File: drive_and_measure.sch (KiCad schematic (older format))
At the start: 39 parts, among them J10 Conn_Coaxial, J17 Conn_Coaxial, J2 7461057, J3 7461057, J4 7461057, J5 7461057, Q1 2SC5242, Q2 2SC5242, Q3 2SD882, U2 INA240A2D, U5 OPA188xxDBV

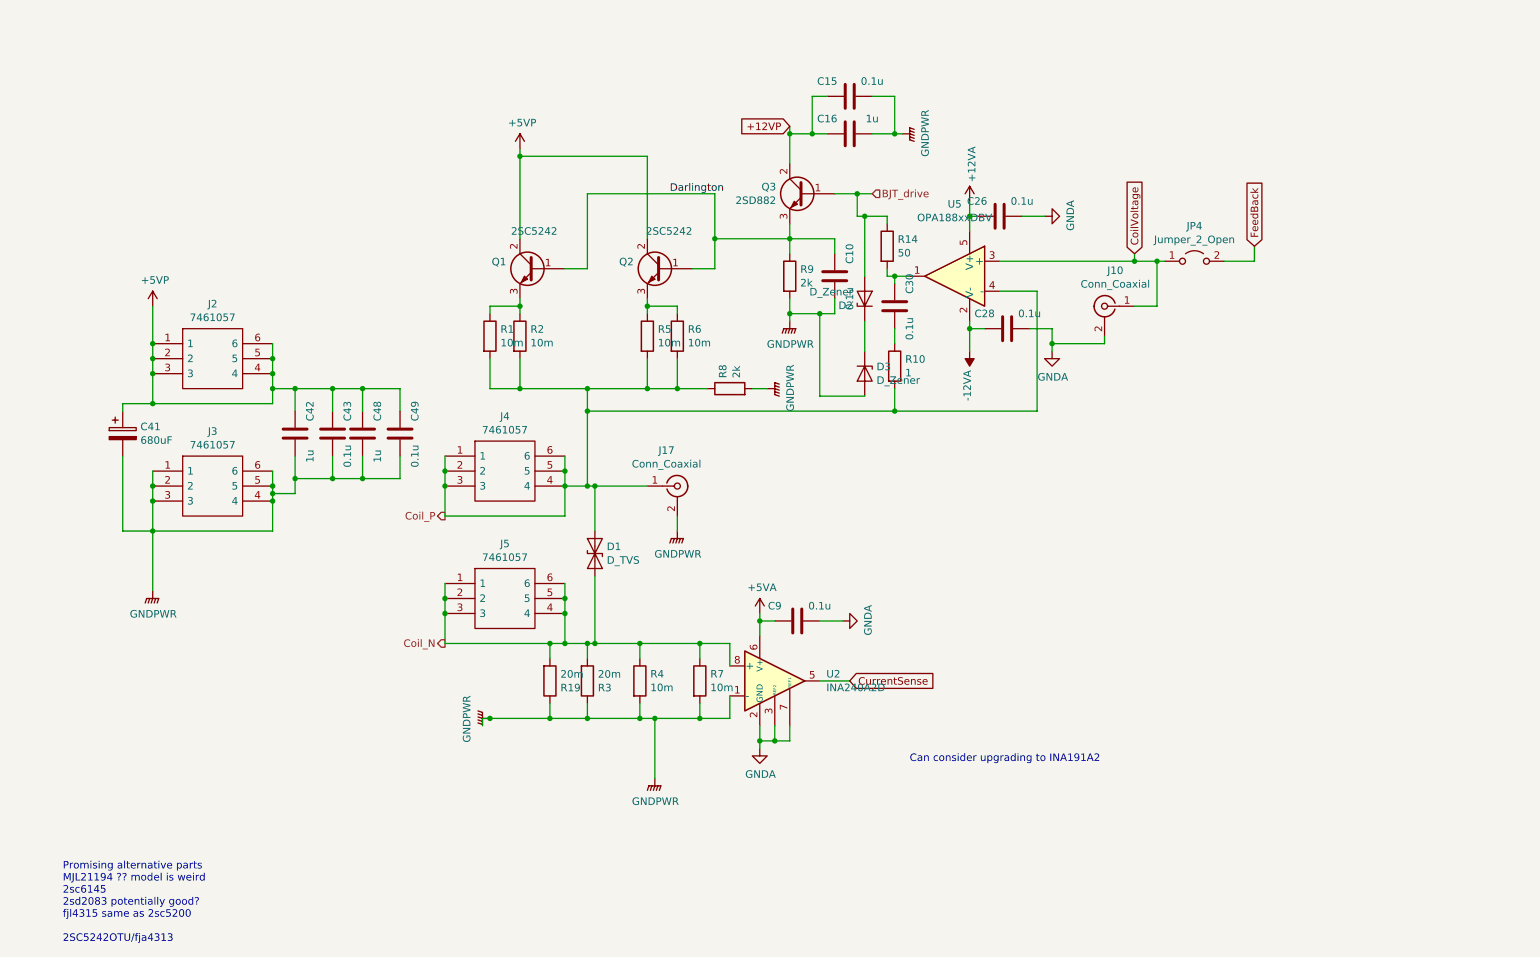
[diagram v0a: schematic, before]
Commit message: Updated design, to include proper feedback and a current bias. Note the sign of the feedback might still be problematic. Need to be checked again
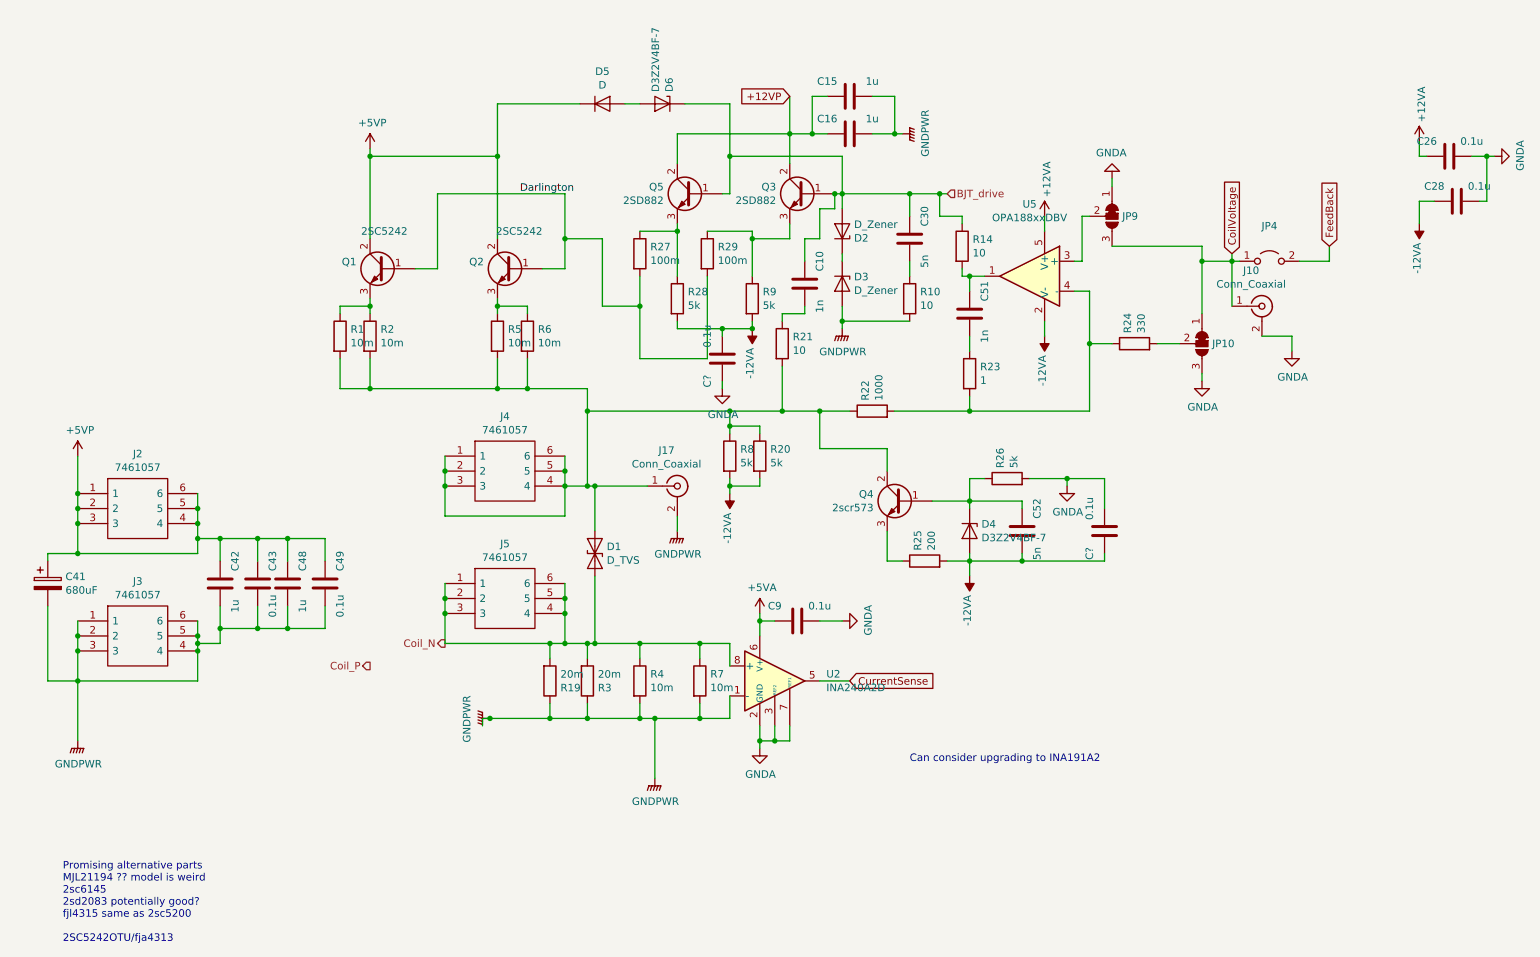
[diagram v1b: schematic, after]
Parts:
- added C51: 1n, Capacitor_SMD:C_1206_3216Metric, symbol Device:C
- added C52: 5n, Capacitor_SMD:C_1206_3216Metric, symbol Device:C
- added C? (x2): 0.1u, Capacitor_SMD:C_0805_2012Metric_Pad1.15x1.40mm_HandSolder, symbol Device:C
- added D4, D6: D3Z2V4BF-7, Diode_SMD:D_SOD-323, symbol Device:D_Zener
- added D5: D, Diode_SMD:D_SOD-323, symbol Device:D
- added JP10, JP9: SolderJumper_3_Bridged12, Jumper:SolderJumper-3_P1.3mm_Bridged12_RoundedPad1.0x1.5mm, symbol Jumper:SolderJumper_3_Bridged12
- added Q4: 2scr573, Package_TO_SOT_SMD:TO-252-2, symbol Device:Q_NPN_BCE
- added Q5: 2SD882, Package_TO_SOT_THT:TO-126-3_Horizontal_TabDown, symbol Device:Q_NPN_BCE
- added R20, R26, R28: 5k, Resistor_SMD:R_1206_3216Metric_Pad1.42x1.75mm_HandSolder, symbol Device:R
- added R21: 10, Resistor_SMD:R_1206_3216Metric_Pad1.42x1.75mm_HandSolder, symbol Device:R
- added R22: 1000, Resistor_SMD:R_1206_3216Metric_Pad1.42x1.75mm_HandSolder, symbol Device:R
- added R23: 1, Resistor_SMD:R_1206_3216Metric_Pad1.42x1.75mm_HandSolder, symbol Device:R
- added R24: 330, Resistor_SMD:R_1206_3216Metric_Pad1.42x1.75mm_HandSolder, symbol Device:R
- added R25: 200, Resistor_SMD:R_1206_3216Metric_Pad1.42x1.75mm_HandSolder, symbol Device:R
- added R27, R29: 100m, Resistor_SMD:R_1206_3216Metric_Pad1.42x1.75mm_HandSolder, symbol Device:R
- C10: value 0.1u -> 1n
- C15: value 0.1u -> 1u; footprint Capacitor_SMD:C_0805_2012Metric_Pad1.15x1.40mm_HandSolder -> Capacitor_SMD:C_1206_3216Metric_Pad1.42x1.75mm_HandSolder
- C30: value 0.1u -> 5n
- Q1, Q2: footprint Package_TO_SOT_THT:TO-3P-3_Horizontal_TabDown -> Package_TO_SOT_THT:TO-3P-3_Vertical
- R10: value 1 -> 10
- R14: value 50 -> 10
- R8, R9: value 2k -> 5k
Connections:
- net +12VP: now also Q5.2 (C)
- net +5VP: now also D5.1 (K)
- net -12VA: now also R8.2, R9.2, C52.1, C?.1, C?.2, D4.2 (A), R20.2, R25.2, R28.2
- net BJT_drive: now also C10.2, C30.2, D6.1 (K), Q5.1 (B)
- net CoilVoltage: now also JP10.1 (A), JP9.3 (B); no longer U5.3 (+)
- net Coil_P: no longer D1.1 (A1), J17.1 (In), J4.1, J4.2, J4.3, J4.4, J4.5, J4.6, R1.2, R10.2, R2.2, R5.2, R6.2, R8.1, U5.4 (-)
- net Darlington: now also R27.2, R29.2; no longer C10.2, Q3.3 (E), R9.1
- net GNDA: now also C?.1, C?.2, JP10.3 (B), JP9.1 (A), R26.2
- net GNDPWR: now also R10.2; no longer C10.1, R8.2, R9.2
- net at R14.2, U5.1: now also C51.2; no longer C30.2
- new net: D1.1 (A1), J17.1 (In), J4.1, J4.2, J4.3, J4.4, J4.5, J4.6, Q4.2 (C), R1.2, R2.2, R20.1, R21.2, R22.1, R5.2, R6.2, R8.1
- new net: Q3.3 (E), R29.1, R9.1
- new net: JP9.2 (C), U5.3 (+)
- new net: R22.2, R23.2, R24.1, U5.4 (-)
- new net: JP10.2 (C), R24.2
- new net: C51.1, R23.1
- new net: D5.2 (A), D6.2 (A)
- new net: C10.1, R21.1
- new net: C52.2, D4.1 (K), Q4.1 (B), R26.1
- new net: Q4.3 (E), R25.1
- new net: Q5.3 (E), R27.1, R28.1
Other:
- moved on the sheet: C26, C28, C41, C42, C43, C48, C49, D2, D3, J10, J2, J3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

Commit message: Allowed swapping feedback signs
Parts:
- added C?: 680uF, Capacitor_THT:CP_Radial_D8.0mm_P3.80mm, symbol Device:CP
- gave numbers to parts that had none: 2
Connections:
- net Coil_P: now also D1.1 (A1), J17.1 (In), J4.1, J4.2, J4.3, J4.4, J4.5, J4.6, Q4.2 (C), R1.2, R2.2, R20.1, R21.2, R22.1, R5.2, R6.2, R8.1
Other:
- moved on the sheet: C41, C42, C43, C48, C49, J2, J3

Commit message: Design a common-mode choke / filter for the controller analog supplies. Avoid using one AC/DC converter for each board, but also suppress ground loops
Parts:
- C41: footprint Capacitor_THT:CP_Radial_D8.0mm_P3.80mm -> SamacSys_Parts:CP_Radial_D10.0mm_P3.5_5
- C55: renamed from C?; value 680uF -> 2000uF; footprint Capacitor_THT:CP_Radial_D8.0mm_P3.80mm -> Capacitor_THT:CP_Radial_D10.0mm_P5.00mm
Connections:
- net +5VP: now also C55.1
- net GNDPWR: now also C55.2
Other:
- moved on the sheet: C55
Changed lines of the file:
@@
 EESchema Schematic File Version 4
-LIBS:shunt_current_control_v2-cache
 EELAYER 30 0
 EELAYER END
@@
 F 0 "C41" H 1168 4496 50  0000 L CNN
 F 1 "680uF" H 1168 4405 50  0000 L CNN
-F 2 "Capacitor_THT:CP_Radial_D8.0mm_P3.80mm" H 1088 4300 50  0001 C CNN
+F 2 "SamacSys_Parts:CP_Radial_D10.0mm_P3.5_5" H 1088 4300 50  0001 C CNN
 F 3 "~" H 1050 4450 50  0001 C CNN
 	1    1050 4450
@@
 	5300 3100 5300 3150
 $Comp
-L Device:CP C?
+L Device:CP C55
 U 1 1 613DA228
-P 700 4450
-F 0 "C?" H 818 4496 50  0000 L CNN
-F 1 "680uF" H 818 4405 50  0000 L CNN
-F 2 "Capacitor_THT:CP_Radial_D8.0mm_P3.80mm" H 738 4300 50  0001 C CNN
-F 3 "~" H 700 4450 50  0001 C CNN
-	1    700  4450
-	1    0    0    -1
-$EndComp
+P 650 4650
+F 0 "C55" H 768 4696 50  0000 L CNN
+F 1 "2000uF" H 768 4605 50  0000 L CNN
+F 2 "Capacitor_THT:CP_Radial_D10.0mm_P5.00mm" H 688 4500 50  0001 C CNN
+F 3 "~" H 650 4650 50  0001 C CNN
+	1    650  4650
+	1    0    0    -1
+$EndComp
+Wire Wire Line
+	650  5100 1050 5100
+Connection ~ 1050 5100
+Wire Wire Line
+	650  4800 650  5100
+Wire Wire Line
+	650  4500 650  4250
+Wire Wire Line
+	650  4250 1050 4250
+Connection ~ 1050 4250
 $EndSCHEMATC

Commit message: Relay array board; Last checkup; Gerberfile updates
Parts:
- D2, D3, D4, D5, D6: footprint Diode_SMD:D_SOD-323 -> Diode_SMD:D_SOD-323_HandSoldering
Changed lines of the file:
@@
 EESchema Schematic File Version 4
+LIBS:shunt_current_control_v2-cache
 EELAYER 30 0
 EELAYER END
@@
 F 0 "D3" V 6054 2529 50  0000 L CNN
 F 1 "D_Zener" V 6145 2529 50  0000 L CNN
-F 2 "Diode_SMD:D_SOD-323" H 6100 2450 50  0001 C CNN
+F 2 "Diode_SMD:D_SOD-323_HandSoldering" H 6100 2450 50  0001 C CNN
 F 3 "~" H 6100 2450 50  0001 C CNN
 	1    6100 2450
@@
 F 0 "D2" V 6054 2179 50  0000 L CNN
 F 1 "D_Zener" V 6145 2179 50  0000 L CNN
-F 2 "Diode_SMD:D_SOD-323" H 6100 2100 50  0001 C CNN
+F 2 "Diode_SMD:D_SOD-323_HandSoldering" H 6100 2100 50  0001 C CNN
 F 3 "~" H 6100 2100 50  0001 C CNN
 	1    6100 2100
@@
 F 0 "D4" V 6904 4179 50  0000 L CNN
 F 1 "D3Z2V4BF-7" V 6995 4179 50  0000 L CNN
-F 2 "Diode_SMD:D_SOD-323" H 6950 4100 50  0001 C CNN
+F 2 "Diode_SMD:D_SOD-323_HandSoldering" H 6950 4100 50  0001 C CNN
 F 3 "~" H 6950 4100 50  0001 C CNN
 	1    6950 4100
@@
 F 0 "D6" V 4854 1329 50  0000 L CNN
 F 1 "D3Z2V4BF-7" V 4945 1329 50  0000 L CNN
-F 2 "Diode_SMD:D_SOD-323" H 4900 1250 50  0001 C CNN
+F 2 "Diode_SMD:D_SOD-323_HandSoldering" H 4900 1250 50  0001 C CNN
 F 3 "~" H 4900 1250 50  0001 C CNN
 	1    4900 1250
@@
 F 0 "D5" H 4500 1466 50  0000 C CNN
 F 1 "D" H 4500 1375 50  0000 C CNN
-F 2 "Diode_SMD:D_SOD-323" H 4500 1250 50  0001 C CNN
+F 2 "Diode_SMD:D_SOD-323_HandSoldering" H 4500 1250 50  0001 C CNN
 F 3 "~" H 4500 1250 50  0001 C CNN
 	1    4500 1250
